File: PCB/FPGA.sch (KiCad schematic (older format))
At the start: 0 parts

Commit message: Worked on PCB, added FPGA.
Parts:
- added C10, C11, C12, C13, C14, C15, C16, C17, C18, C19, C20, C21, C22, C23, C8, C9: 0.1uF, Capacitors_SMD:C_0805_HandSoldering, symbol C
- added P1: CONN_01X05, symbol CONN_01X05
- added U6: LCMX02-640UHC-4TG144C, SMD_Packages:TQFP-144, symbol LCMX02-640UHC-4TG144C
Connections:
- new net +3V3: C10.2, C11.2, C12.2, C13.2, C14.2, C15.2, C16.2, C17.2, C18.2, C19.2, C20.2, C21.2, C22.2, C23.2, C8.2, C9.2, U6.102 (VCCIO1), U6.108 (VCC), U6.118 (VCCIO0), U6.123 (VCCIO0), U6.135 (VCCIO0), U6.144 (VCC), U6.16 (VCCIO3), U6.30 (VCCIO3), U6.36 (VCC), U6.37 (VCCIO2), U6.51 (VCCIO2), U6.66 (VCCIO2), U6.7 (VCCIO3), U6.72 (VCC), U6.79 (VCCIO1), U6.88 (VCCIO1)
- new net CLK: U6.111 (PT17B)
- new net CS_Clock: U6.112 (PT17A)
- new net CS_Encoder: U6.114 (PT16C)
- new net CS_PWM: U6.113 (PT16D)
- new net DataIN: U6.109 (PT17D)
- new net DataOUT: U6.110 (PT17C)
- new net GND: C10.1, C11.1, C12.1, C13.1, C14.1, C15.1, C16.1, C17.1, C18.1, C19.1, C20.1, C21.1, C22.1, C23.1, C8.1, C9.1, P1.5 (P5), U6.101 (GND), U6.116 (GND), U6.124 (GND), U6.134 (GND), U6.18 (GND), U6.29 (GND), U6.46 (GND), U6.53 (GND), U6.64 (GND), U6.8 (GND), U6.80 (GND), U6.90 (GND)
- new net SCL: U6.126 (PT12C)
- new net SDA: U6.125 (PT12D)
- new net TCK: P1.3 (P3), U6.131 (PT11C/TCK)
- new net TDI: P1.2 (P2), U6.136 (PT10D/TDI)
- new net TDO: P1.1 (P1), U6.137 (PT10C/TDO)
- new net TMS: P1.4 (P4), U6.130 (PT11D/TMS)

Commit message: Worked on PCB.
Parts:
- C10, C11, C12, C13, C14, C15, C16, C17, C18, C19, C20, C21, C22, C23, C8, C9: footprint Capacitors_SMD:C_0805_HandSoldering -> Capacitors_SMD:C_0603_HandSoldering
- U6: footprint SMD_Packages:TQFP-144 -> Housings_QFP:TQFP-144_20x20mm_Pitch0.5mm
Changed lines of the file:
@@
 F 0 "U6" H 2550 2200 60  0000 C CNN
 F 1 "LCMX02-640UHC-4TG144C" V 2900 4550 60  0000 C CNN
-F 2 "SMD_Packages:TQFP-144" H 2650 3550 60  0001 C CNN
+F 2 "Housings_QFP:TQFP-144_20x20mm_Pitch0.5mm" H 2650 3550 60  0001 C CNN
 F 3 "" H 2650 3550 60  0000 C CNN
 	1    2550 3800
@@
 F 0 "U6" H 4550 2200 60  0000 C CNN
 F 1 "LCMX02-640UHC-4TG144C" V 4900 4550 60  0000 C CNN
-F 2 "SMD_Packages:TQFP-144" H 4650 3550 60  0001 C CNN
+F 2 "Housings_QFP:TQFP-144_20x20mm_Pitch0.5mm" H 4650 3550 60  0001 C CNN
 F 3 "" H 4650 3550 60  0000 C CNN
 	2    4550 3800
@@
 F 0 "U6" H 6550 2200 60  0000 C CNN
 F 1 "LCMX02-640UHC-4TG144C" V 6900 4550 60  0000 C CNN
-F 2 "SMD_Packages:TQFP-144" H 6600 1550 60  0001 C CNN
+F 2 "Housings_QFP:TQFP-144_20x20mm_Pitch0.5mm" H 6600 1550 60  0001 C CNN
 F 3 "" H 6650 3550 60  0000 C CNN
 	3    6550 3800
@@
 F 0 "U6" H 8550 2200 60  0000 C CNN
 F 1 "LCMX02-640UHC-4TG144C" V 8900 4550 60  0000 C CNN
-F 2 "SMD_Packages:TQFP-144" H 8650 3550 60  0001 C CNN
+F 2 "Housings_QFP:TQFP-144_20x20mm_Pitch0.5mm" H 8650 3550 60  0001 C CNN
 F 3 "" H 8650 3550 60  0000 C CNN
 	4    8550 3800
@@
 F 0 "U6" H 10550 2200 60  0000 C CNN
 F 1 "LCMX02-640UHC-4TG144C" V 10900 4550 60  0000 C CNN
-F 2 "SMD_Packages:TQFP-144" H 10650 3550 60  0001 C CNN
+F 2 "Housings_QFP:TQFP-144_20x20mm_Pitch0.5mm" H 10650 3550 60  0001 C CNN
 F 3 "" H 10650 3550 60  0000 C CNN
 	5    10550 3800
@@
 F 0 "C10" H 4500 1250 40  0000 L CNN
 F 1 "0.1uF" H 4506 1065 40  0000 L CNN
-F 2 "Capacitors_SMD:C_0805_HandSoldering" H 4538 1000 30  0001 C CNN
+F 2 "Capacitors_SMD:C_0603_HandSoldering" H 4538 1000 30  0001 C CNN
 F 3 "" H 4500 1150 60  0000 C CNN
 	1    4500 1150
@@
 F 0 "C9" H 4250 1250 40  0000 L CNN
 F 1 "0.1uF" H 4256 1065 40  0000 L CNN
-F 2 "Capacitors_SMD:C_0805_HandSoldering" H 4288 1000 30  0001 C CNN
+F 2 "Capacitors_SMD:C_0603_HandSoldering" H 4288 1000 30  0001 C CNN
 F 3 "" H 4250 1150 60  0000 C CNN
 	1    4250 1150
@@
 F 0 "C8" H 4000 1250 40  0000 L CNN
 F 1 "0.1uF" H 4006 1065 40  0000 L CNN
-F 2 "Capacitors_SMD:C_0805_HandSoldering" H 4038 1000 30  0001 C CNN
+F 2 "Capacitors_SMD:C_0603_HandSoldering" H 4038 1000 30  0001 C CNN
 F 3 "" H 4000 1150 60  0000 C CNN
 	1    4000 1150
@@
 F 0 "C11" H 4750 1250 40  0000 L CNN
 F 1 "0.1uF" H 4756 1065 40  0000 L CNN
-F 2 "Capacitors_SMD:C_0805_HandSoldering" H 4788 1000 30  0001 C CNN
+F 2 "Capacitors_SMD:C_0603_HandSoldering" H 4788 1000 30  0001 C CNN
 F 3 "" H 4750 1150 60  0000 C CNN
 	1    4750 1150
@@
 F 0 "C12" H 5550 1250 40  0000 L CNN
 F 1 "0.1uF" H 5556 1065 40  0000 L CNN
-F 2 "Capacitors_SMD:C_0805_HandSoldering" H 5588 1000 30  0001 C CNN
+F 2 "Capacitors_SMD:C_0603_HandSoldering" H 5588 1000 30  0001 C CNN
 F 3 "" H 5550 1150 60  0000 C CNN
 	1    5550 1150
@@
 F 0 "C13" H 5800 1250 40  0000 L CNN
 F 1 "0.1uF" H 5806 1065 40  0000 L CNN
-F 2 "Capacitors_SMD:C_0805_HandSoldering" H 5838 1000 30  0001 C CNN
+F 2 "Capacitors_SMD:C_0603_HandSoldering" H 5838 1000 30  0001 C CNN
 F 3 "" H 5800 1150 60  0000 C CNN
 	1    5800 1150
@@
 F 0 "C14" H 6050 1250 40  0000 L CNN
 F 1 "0.1uF" H 6056 1065 40  0000 L CNN
-F 2 "Capacitors_SMD:C_0805_HandSoldering" H 6088 1000 30  0001 C CNN
+F 2 "Capacitors_SMD:C_0603_HandSoldering" H 6088 1000 30  0001 C CNN
 F 3 "" H 6050 1150 60  0000 C CNN
 	1    6050 1150
@@
 F 0 "C15" H 6850 1250 40  0000 L CNN
 F 1 "0.1uF" H 6856 1065 40  0000 L CNN
-F 2 "Capacitors_SMD:C_0805_HandSoldering" H 6888 1000 30  0001 C CNN
+F 2 "Capacitors_SMD:C_0603_HandSoldering" H 6888 1000 30  0001 C CNN
 F 3 "" H 6850 1150 60  0000 C CNN
 	1    6850 1150
@@
 F 0 "C16" H 7100 1250 40  0000 L CNN
 F 1 "0.1uF" H 7106 1065 40  0000 L CNN
-F 2 "Capacitors_SMD:C_0805_HandSoldering" H 7138 1000 30  0001 C CNN
+F 2 "Capacitors_SMD:C_0603_HandSoldering" H 7138 1000 30  0001 C CNN
 F 3 "" H 7100 1150 60  0000 C CNN
 	1    7100 1150
@@
 F 0 "C17" H 7350 1250 40  0000 L CNN
 F 1 "0.1uF" H 7356 1065 40  0000 L CNN
-F 2 "Capacitors_SMD:C_0805_HandSoldering" H 7388 1000 30  0001 C CNN
+F 2 "Capacitors_SMD:C_0603_HandSoldering" H 7388 1000 30  0001 C CNN
 F 3 "" H 7350 1150 60  0000 C CNN
 	1    7350 1150
@@
 F 0 "C18" H 8100 1250 40  0000 L CNN
 F 1 "0.1uF" H 8106 1065 40  0000 L CNN
-F 2 "Capacitors_SMD:C_0805_HandSoldering" H 8138 1000 30  0001 C CNN
+F 2 "Capacitors_SMD:C_0603_HandSoldering" H 8138 1000 30  0001 C CNN
 F 3 "" H 8100 1150 60  0000 C CNN
 	1    8100 1150
@@
 F 0 "C19" H 8350 1250 40  0000 L CNN
 F 1 "0.1uF" H 8356 1065 40  0000 L CNN
-F 2 "Capacitors_SMD:C_0805_HandSoldering" H 8388 1000 30  0001 C CNN
+F 2 "Capacitors_SMD:C_0603_HandSoldering" H 8388 1000 30  0001 C CNN
 F 3 "" H 8350 1150 60  0000 C CNN
 	1    8350 1150
@@
 F 0 "C20" H 8600 1250 40  0000 L CNN
 F 1 "0.1uF" H 8606 1065 40  0000 L CNN
-F 2 "Capacitors_SMD:C_0805_HandSoldering" H 8638 1000 30  0001 C CNN
+F 2 "Capacitors_SMD:C_0603_HandSoldering" H 8638 1000 30  0001 C CNN
 F 3 "" H 8600 1150 60  0000 C CNN
 	1    8600 1150
@@
 F 0 "C21" H 9400 1250 40  0000 L CNN
 F 1 "0.1uF" H 9406 1065 40  0000 L CNN
-F 2 "Capacitors_SMD:C_0805_HandSoldering" H 9438 1000 30  0001 C CNN
+F 2 "Capacitors_SMD:C_0603_HandSoldering" H 9438 1000 30  0001 C CNN
 F 3 "" H 9400 1150 60  0000 C CNN
 	1    9400 1150
@@
 F 0 "C22" H 9650 1250 40  0000 L CNN
 F 1 "0.1uF" H 9656 1065 40  0000 L CNN
-F 2 "Capacitors_SMD:C_0805_HandSoldering" H 9688 1000 30  0001 C CNN
+F 2 "Capacitors_SMD:C_0603_HandSoldering" H 9688 1000 30  0001 C CNN
 F 3 "" H 9650 1150 60  0000 C CNN
 	1    9650 1150
@@
 F 0 "C23" H 9900 1250 40  0000 L CNN
 F 1 "0.1uF" H 9906 1065 40  0000 L CNN
-F 2 "Capacitors_SMD:C_0805_HandSoldering" H 9938 1000 30  0001 C CNN
+F 2 "Capacitors_SMD:C_0603_HandSoldering" H 9938 1000 30  0001 C CNN
 F 3 "" H 9900 1150 60  0000 C CNN
 	1    9900 1150

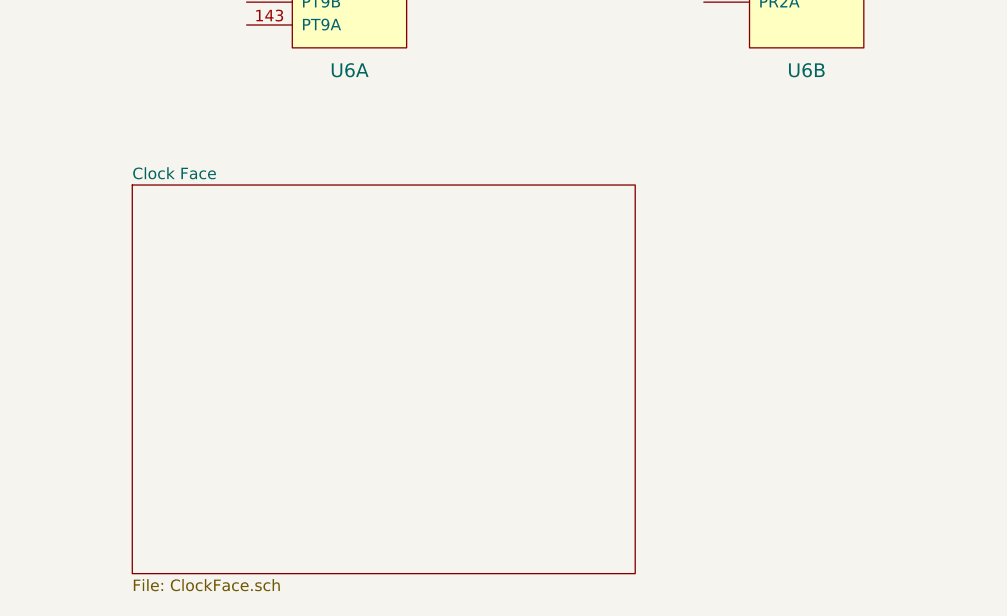
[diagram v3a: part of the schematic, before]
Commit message: Finished LED array footprint.
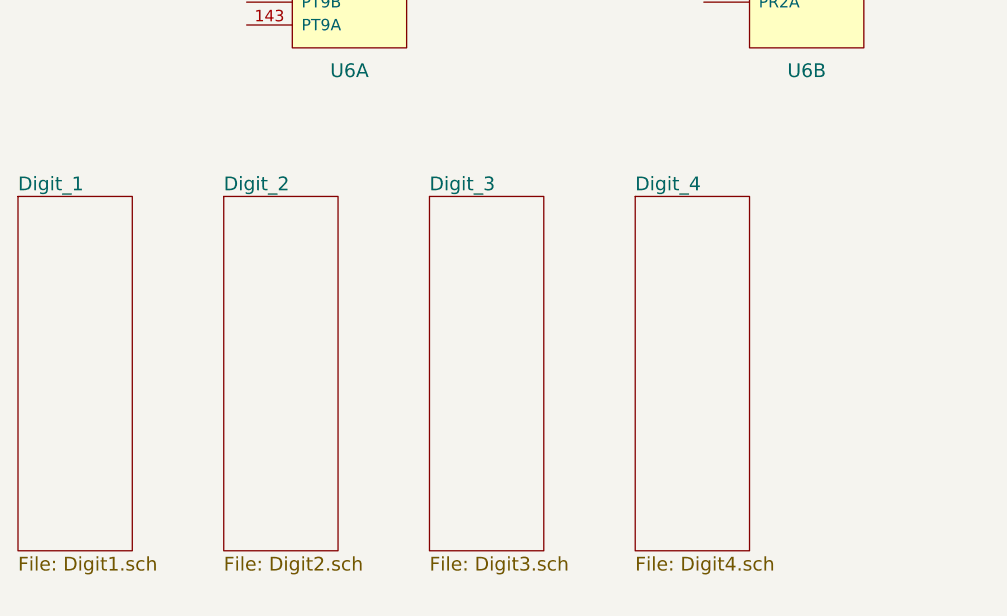
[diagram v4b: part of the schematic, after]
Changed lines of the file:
@@
 $Descr A4 11693 8268
 encoding utf-8
-Sheet 2 3
+Sheet 2 6
 Title "4 Digit 7 Segment Clock"
 Date "12/27/14"
@@
 Text GLabel 1950 3800 0    50   Input ~ 0
 SCL
-$Sheet
-S 1600 5900 2200 1700
-U 54B63892
-F0 "Clock Face" 50
-F1 "ClockFace.sch" 50
-$EndSheet
 $Bitmap
 Pos 10200 6850
@@
 EndData
 $EndBitmap
+$Sheet
+S 2000 5950 500  1550
+U 54BC7562
+F0 "Digit_2" 60
+F1 "Digit2.sch" 60
+$EndSheet
+$Sheet
+S 2900 5950 500  1550
+U 54BC757D
+F0 "Digit_3" 60
+F1 "Digit3.sch" 60
+$EndSheet
+$Sheet
+S 3800 5950 500  1550
+U 54BC7598
+F0 "Digit_4" 60
+F1 "Digit4.sch" 60
+$EndSheet
+$Sheet
+S 1100 5950 500  1550
+U 54BC74C5
+F0 "Digit_1" 60
+F1 "Digit1.sch" 60
+$EndSheet
 $EndSCHEMATC

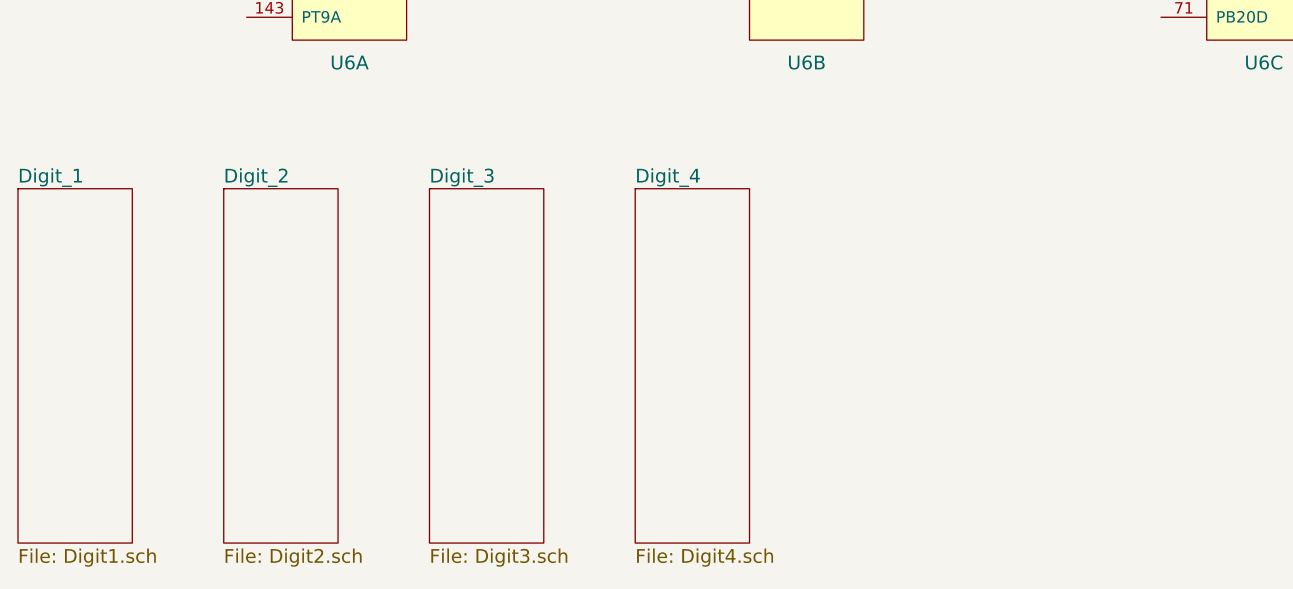
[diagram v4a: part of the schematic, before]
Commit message: Added additional mosfets.
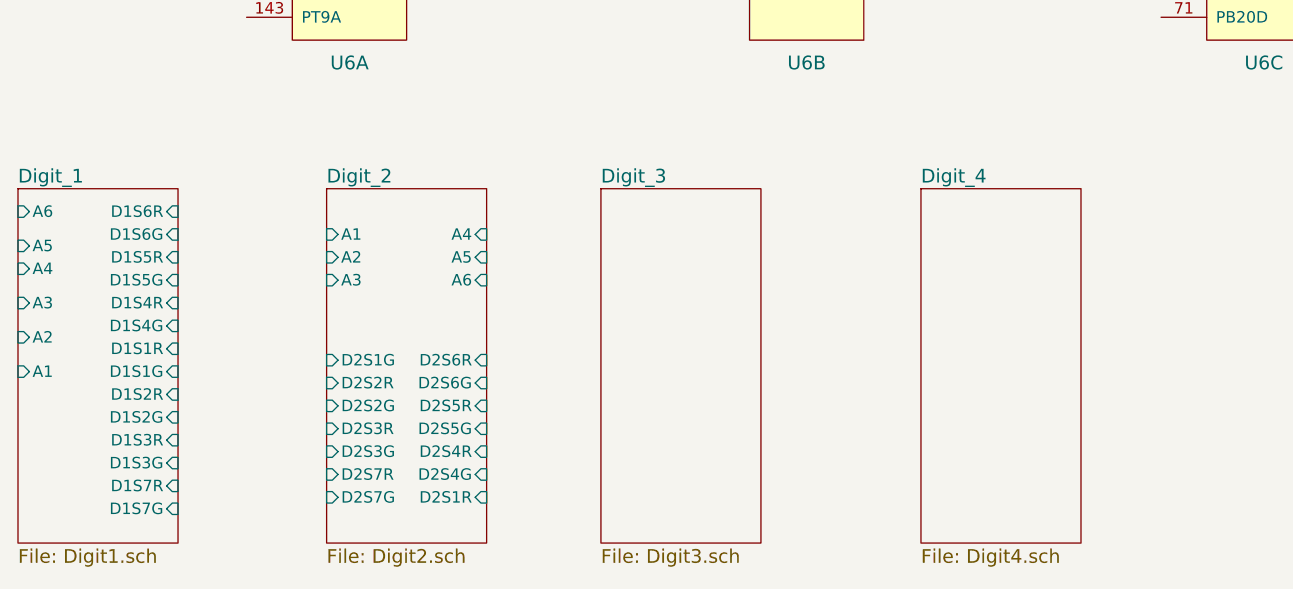
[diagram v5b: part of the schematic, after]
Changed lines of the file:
@@
 $EndBitmap
 $Sheet
-S 2000 5950 500  1550
-U 54BC7562
-F0 "Digit_2" 60
-F1 "Digit2.sch" 60
-$EndSheet
-$Sheet
-S 2900 5950 500  1550
+S 3650 5950 700  1550
 U 54BC757D
 F0 "Digit_3" 60
@@
 $EndSheet
 $Sheet
-S 3800 5950 500  1550
+S 5050 5950 700  1550
 U 54BC7598
 F0 "Digit_4" 60
@@
 $EndSheet
 $Sheet
-S 1100 5950 500  1550
+S 1100 5950 700  1550
 U 54BC74C5
 F0 "Digit_1" 60
 F1 "Digit1.sch" 60
+F2 "D1S6R" I R 1800 6050 50
+F3 "D1S6G" I R 1800 6150 50
+F4 "D1S5R" I R 1800 6250 50
+F5 "D1S5G" I R 1800 6350 50
+F6 "D1S4R" I R 1800 6450 50
+F7 "D1S4G" I R 1800 6550 50
+F8 "D1S1R" I R 1800 6650 50
+F9 "D1S1G" I R 1800 6750 50
+F10 "D1S2R" I R 1800 6850 50
+F11 "D1S2G" I R 1800 6950 50
+F12 "D1S3R" I R 1800 7050 50
+F13 "D1S3G" I R 1800 7150 50
+F14 "D1S7R" I R 1800 7250 50
+F15 "D1S7G" I R 1800 7350 50
+F16 "A6" I L 1100 6050 50
+F17 "A5" I L 1100 6200 50
+F18 "A4" I L 1100 6300 50
+F19 "A3" I L 1100 6450 50
+F20 "A2" I L 1100 6600 50
+F21 "A1" I L 1100 6750 50
+$EndSheet
+$Sheet
+S 2450 5950 700  1550
+U 54BC7562
+F0 "Digit_2" 60
+F1 "Digit2.sch" 60
+F2 "D2S6R" I R 3150 6700 50
+F3 "D2S6G" I R 3150 6800 50
+F4 "D2S5R" I R 3150 6900 50
+F5 "D2S5G" I R 3150 7000 50
+F6 "D2S4R" I R 3150 7100 50
+F7 "D2S4G" I R 3150 7200 50
+F8 "D2S1R" I R 3150 7300 50
+F9 "D2S1G" I L 2450 6700 50
+F10 "D2S2R" I L 2450 6800 50
+F11 "D2S2G" I L 2450 6900 50
+F12 "D2S3R" I L 2450 7000 50
+F13 "D2S3G" I L 2450 7100 50
+F14 "D2S7R" I L 2450 7200 50
+F15 "D2S7G" I L 2450 7300 50
+F16 "A6" I R 3150 6350 50
+F17 "A5" I R 3150 6250 50
+F18 "A4" I R 3150 6150 50
+F19 "A3" I L 2450 6350 50
+F20 "A2" I L 2450 6250 50
+F21 "A1" I L 2450 6150 50
 $EndSheet
 $EndSCHEMATC

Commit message: Edit PCB.
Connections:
- wire segments 90 -> 170

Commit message: PCB work.
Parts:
- added Q2, Q3, Q4: DMN2041LSD-13, SO-8, symbol DMN2041LSD-13
- added R10, R11, R12, R7, R8, R9: 10K, Resistors_SMD:R_0603_HandSoldering, symbol R
- added R13, R14, R15, R16, R17, R18: 150, Resistors_SMD:R_0603_HandSoldering, symbol R
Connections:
- net labels added: +5V, A1, A2, A3, A4, A5, A6
- wire segments 170 -> 206
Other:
- moved on the sheet: C10, C11, C12, C13, C14, C15, C16, C17, C18, C19, C20, C21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

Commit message: PCB work.
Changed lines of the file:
@@
 $Descr A4 11693 8268
 encoding utf-8
-Sheet 2 6
+Sheet 2 7
 Title "4 Digit 7 Segment Clock"
 Date "12/27/14"
@@
 Text Label 6500 6850 2    50   ~ 0
 A6
+$Sheet
+S 9900 5750 800  500
+U 55B5DB7D
+F0 "Indicators" 60
+F1 "Indicators.sch" 60
+$EndSheet
 $EndSCHEMATC
